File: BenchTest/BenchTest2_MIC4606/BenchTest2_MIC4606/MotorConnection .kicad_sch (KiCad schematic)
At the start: 4 parts, among them J1 7460553, J3 S95243, J4 S95243, J5 7460553

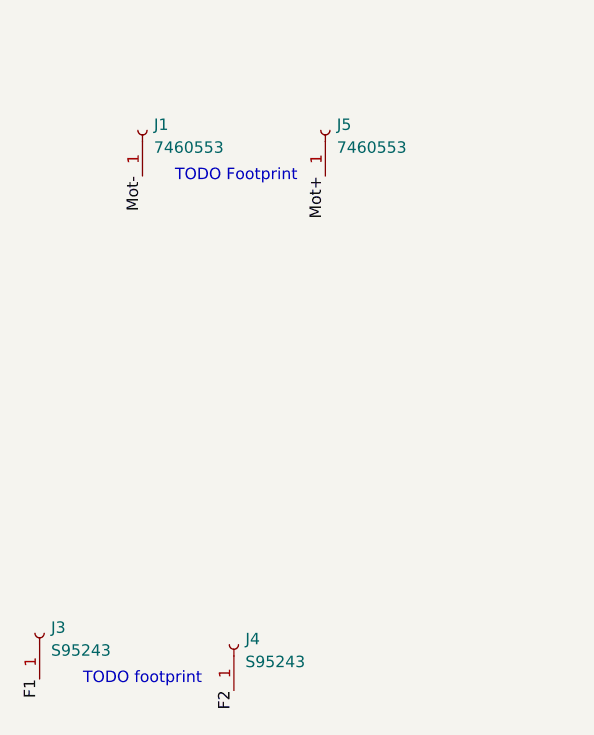
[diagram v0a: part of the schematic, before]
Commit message: Connector Footprints Assigned
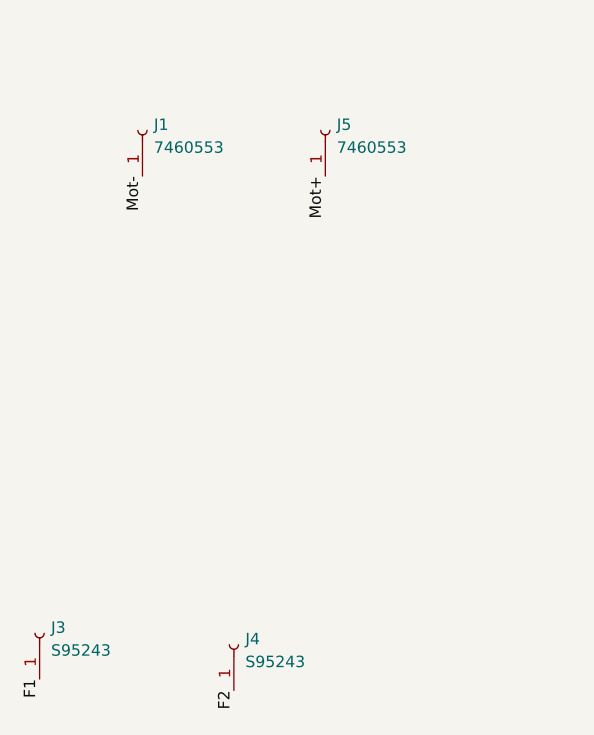
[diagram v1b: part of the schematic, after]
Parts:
- J1, J5: footprint (none) -> Library:WP-BUTR_7460553
- J3, J4: footprint (none) -> Library:S95243
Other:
- note removed: "TODO Footprint"
- note removed: "TODO footprint"
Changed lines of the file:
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@@
 	(generator_version "9.0")
 	(paper "A4")
-	(text "TODO Footprint"
-		(exclude_from_sim no)
-		(at 205.994 85.09 0)
-		(effects
-			(font
-				(size 1.27 1.27)
-			)
-		)
-	)
-	(text "TODO footprint"
-		(exclude_from_sim no)
-		(at 195.58 140.97 0)
-		(effects
-			(font
-				(size 1.27 1.27)
-			)
-		)
-	)
 	(label "Mot+"
 		(at 269.24 19.05 180)
@@
 			)
 		)
-		(property "Footprint" ""
+		(property "Footprint" "Library:WP-BUTR_7460553"
 			(at 195.58 80.01 0)
 			(effects
@@
 			)
 		)
-		(property "Footprint" ""
+		(property "Footprint" "Library:S95243"
 			(at 184.15 135.89 0)
 			(effects
@@
 			)
 		)
-		(property "Footprint" ""
+		(property "Footprint" "Library:WP-BUTR_7460553"
 			(at 215.9 80.01 0)
 			(effects
@@
 			)
 		)
-		(property "Footprint" ""
+		(property "Footprint" "Library:S95243"
 			(at 205.74 137.16 0)
 			(effects
